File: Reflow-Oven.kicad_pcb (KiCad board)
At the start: 2 copper layers, 53 parts, among them J1 Thermocouple 1, J10 Display, J11 GND(A), J12 +12V, J13 Servo 2, J14 Servo 1, J15 Door, J17 Servo 3, J18 Ambient snesor, J19 Controls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

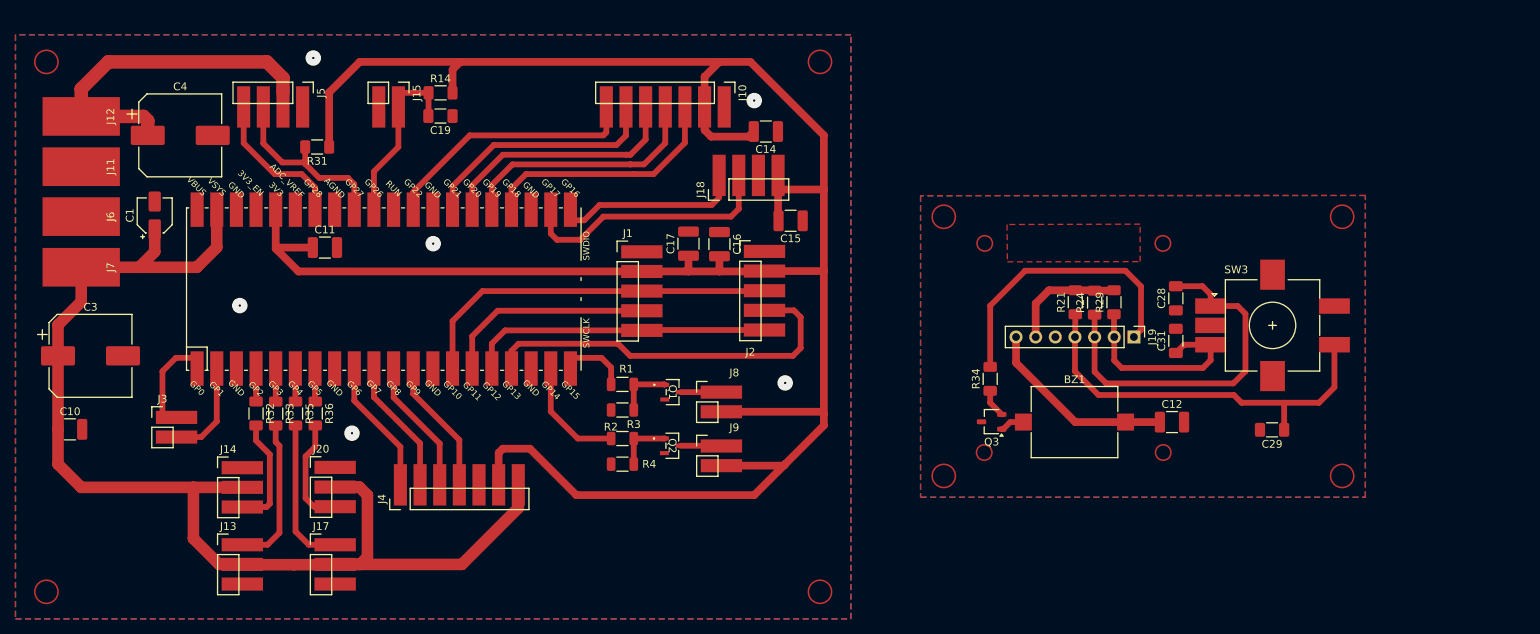
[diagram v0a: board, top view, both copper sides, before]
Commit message: Single servo with cutoff
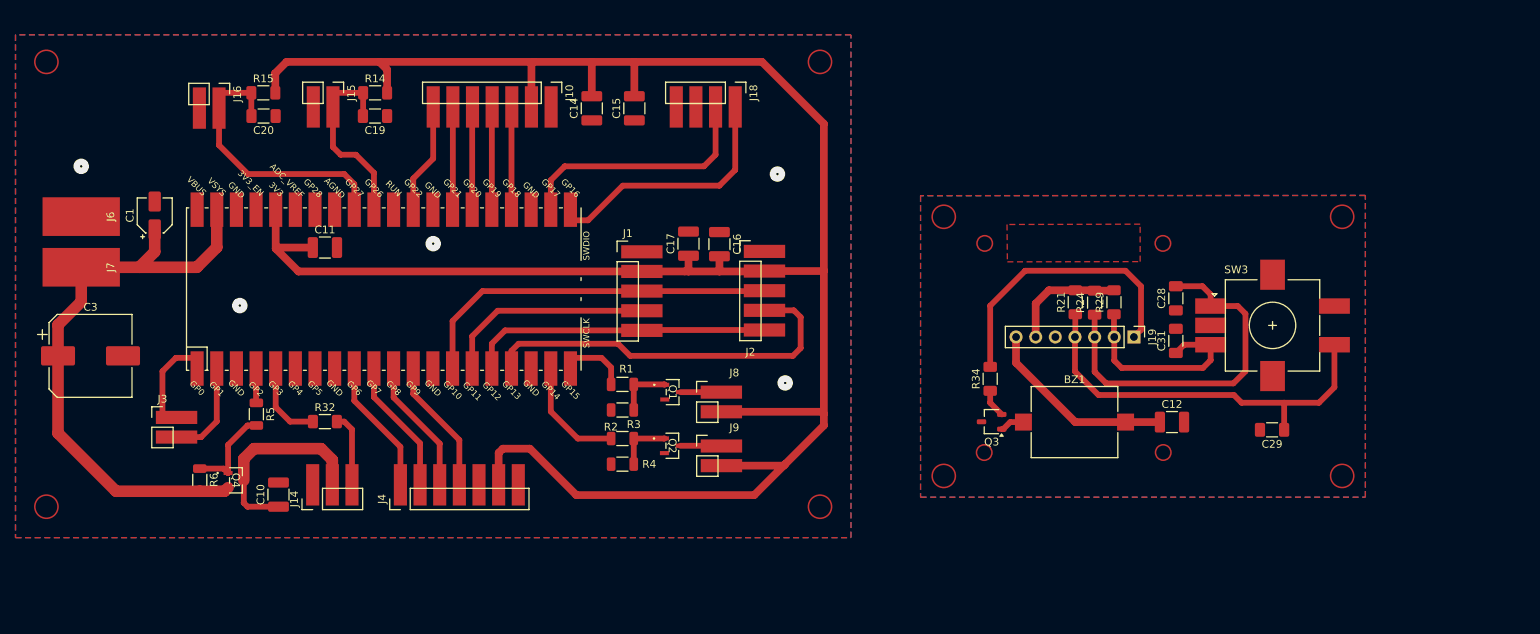
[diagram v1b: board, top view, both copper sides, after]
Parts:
- removed C4: 1000uf, Capacitor_SMD:CP_Elec_10x10.5
- removed J11: GND(A), Connector_Wire:SolderWirePad_1x01_SMD_5x10mm
- removed J12: +12V, Connector_Wire:SolderWirePad_1x01_SMD_5x10mm
- removed J13: Servo 2, Connector_PinHeader_2.54mm:PinHeader_1x03_P2.54mm_Vertical_SMD
- removed J17: Servo 3, Connector_PinHeader_2.54mm:PinHeader_1x03_P2.54mm_Vertical_SMD
- removed J20: Servo 4, Connector_PinHeader_2.54mm:PinHeader_1x03_P2.54mm_Vertical_SMD
- removed J5: Fan, Connector_PinHeader_2.54mm:PinHeader_1x04_P2.54mm_Vertical_SMD
- removed R31: 1K, Resistor_SMD:R_1206_3216Metric_Pad1.30x1.75mm_HandSolder
- removed R33, R35, R36: 220R, Resistor_SMD:R_1206_3216Metric_Pad1.30x1.75mm_HandSolder
- added C20: 10nf, Capacitor_SMD:C_1206_3216Metric_Pad1.33x1.80mm_HandSolder, F.Cu at (113.1, 58.0)
- added J16: Door, Connector_PinHeader_2.54mm:PinHeader_1x02_P2.54mm_Vertical_SMD, F.Cu at (107.3, 55.1)
- added Q4: AO3401A, PMV20XNER:SOT23-TO-236AB_NEX, F.Cu at (109.5, 105.1)
- added R15: 4K7, Resistor_SMD:R_1206_3216Metric_Pad1.30x1.75mm_HandSolder, F.Cu at (113.0, 55.0)
- added R5: 330R, Resistor_SMD:R_1206_3216Metric, F.Cu at (112.1, 96.5)
- added R6: 10K, Resistor_SMD:R_1206_3216Metric, F.Cu at (104.8, 105.0)
- moved C10 28.2 mm to (115.0, 106.9), turned to 90 degrees
- moved C15 24.9 mm to (161.0, 57.0), turned to 90 degrees
- moved C14 22.7 mm to (155.5, 57.0), turned to 90 degrees
- moved J10 22.4 mm to (150.2, 55.0)
- moved J18 12.7 mm to (174.0, 55.0), turned to -90 degrees
- moved J14 11.6 mm to (119.4, 107.5), turned to 90 degrees
- moved R32 8.96 mm to (121.0, 97.5), turned to 0 degrees
- moved C19 8.46 mm to (127.5, 58.0)
- moved J15 8.46 mm to (122.0, 55.0)
- moved R14 8.46 mm to (127.5, 55.0)
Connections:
- net /Door renamed /Door OP
- C10 pad 1: +5V -> Net-(J14-Pin_2)
- J14 pad 2: +5V -> Net-(J14-Pin_2)
- R32 pad 1: /Servo 1 -> /Servo SIG
- U1 pad 32: Net-(J5-Pin_3) -> /Door CL
- U1 pad 34: Net-(J5-Pin_4) -> unconnected-(U1-GPIO28_ADC2-Pad34)
- U1 pad 4: /Servo 1 -> /Servo EN
- U1 pad 5: /Servo 2 -> /Servo SIG
- U1 pad 6: /Servo 3 -> unconnected-(U1-GPIO4-Pad6)
- U1 pad 7: /Servo 4 -> unconnected-(U1-GPIO5-Pad7)
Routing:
- net +5V: track 177.9 -> 100.9 mm
- net +12V: track 44.6 -> 0.00 mm
- net /Door CL: track 0.00 -> 38.1 mm
- net Net-(J14-Pin_2): track 0.00 -> 28.0 mm
- net Net-(J5-Pin_3): track 27.3 -> 0.00 mm
- net Net-(J5-Pin_4): track 22.3 -> 0.00 mm
- net Net-(J13-Pin_1): track 21.3 -> 0.00 mm
- net Net-(J10-Pin_7): track 36.9 -> 17.5 mm
- net Net-(J10-Pin_4): track 35.8 -> 16.6 mm
- net Net-(J10-Pin_3): track 35.5 -> 16.6 mm
- net Net-(J10-Pin_5): track 35.5 -> 16.6 mm
- net Net-(J10-Pin_6): track 35.1 -> 16.6 mm
- net Net-(J17-Pin_1): track 17.7 -> 0.00 mm
- net Net-(J18-Pin_1): track 21.5 -> 34.0 mm
- net Net-(J20-Pin_3): track 12.4 -> 0.00 mm
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
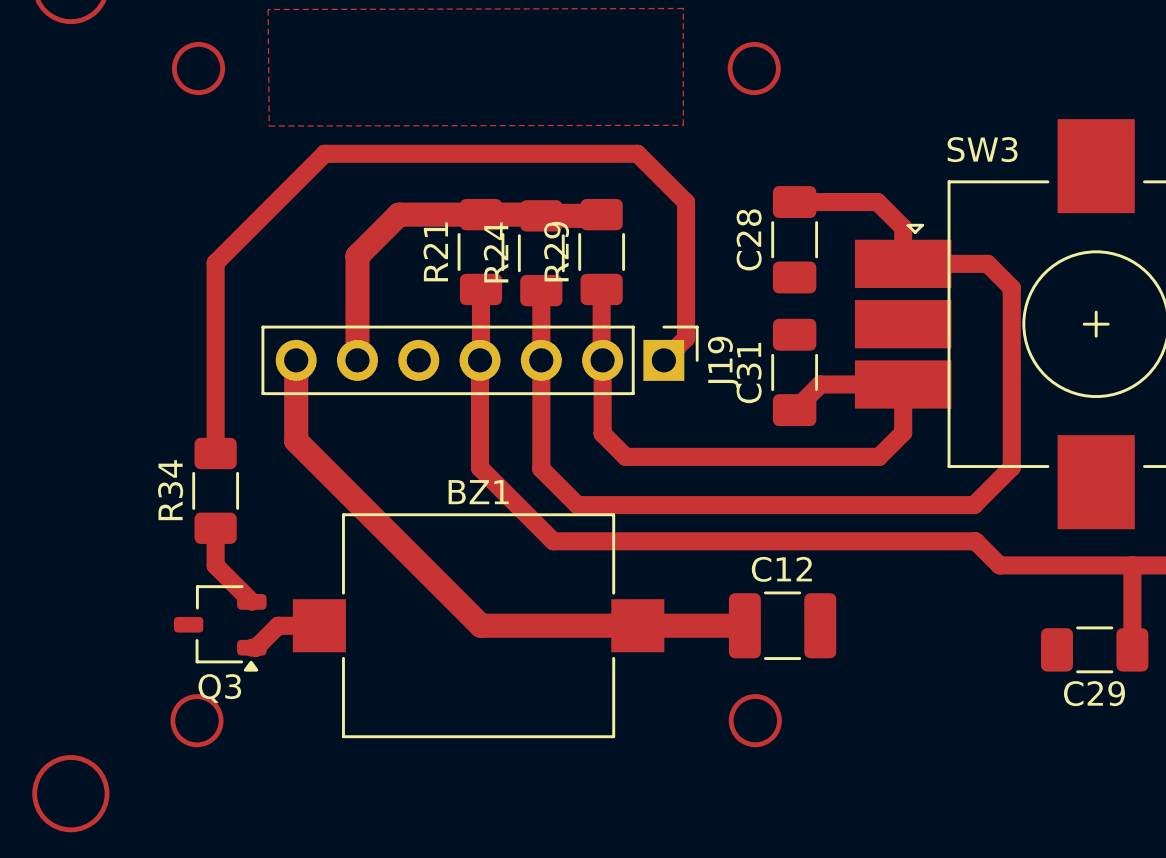
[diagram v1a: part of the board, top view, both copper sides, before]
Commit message: Single servo with cutoff
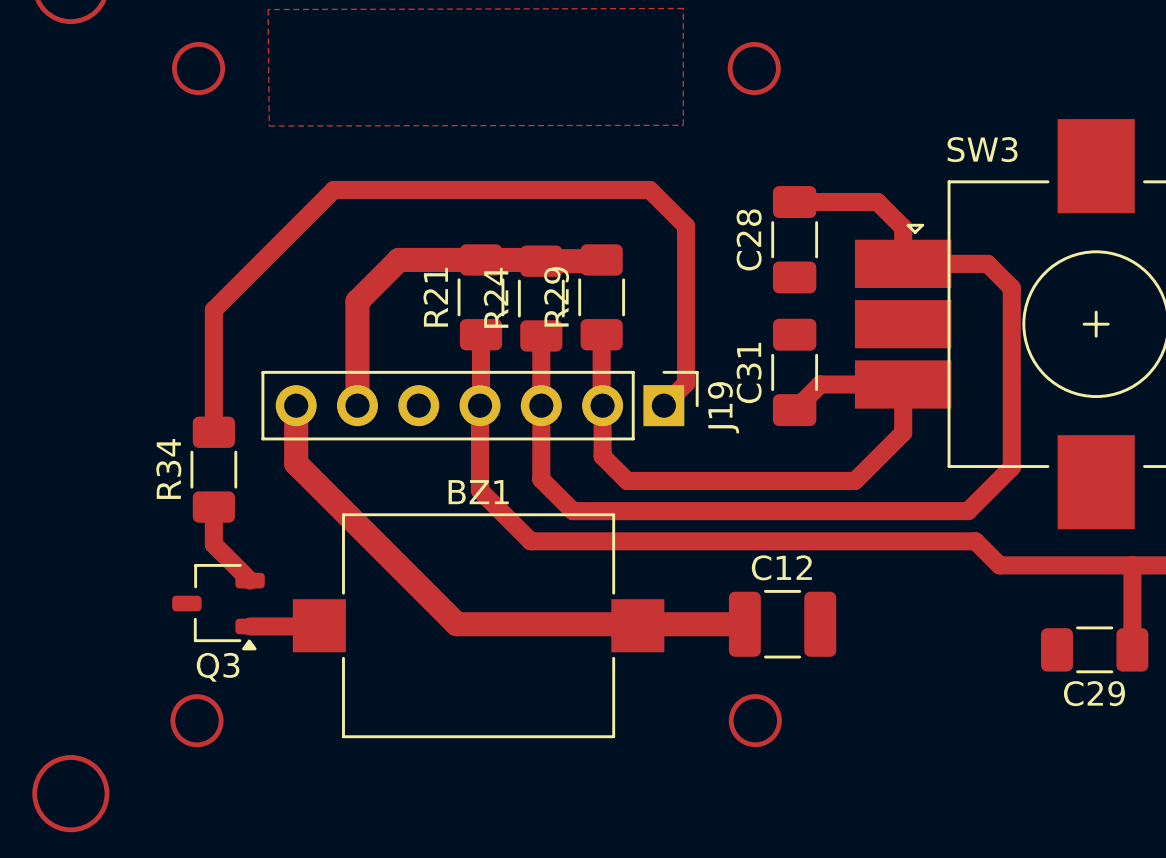
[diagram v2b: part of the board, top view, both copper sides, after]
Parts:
- moved J19 1.88 mm to (225.6, 88.4)
- moved R21 1.88 mm to (218.0, 84.0)
- moved R24 1.88 mm to (220.5, 84.0)
- moved R29 1.88 mm to (223.0, 84.0)
- moved R34 0.88 mm to (206.9, 91.1)
- moved Q3 0.88 mm to (207.1, 96.6)
- moved C12 0.06 mm to (230.5, 97.5)
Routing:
- net Net-(J19-Pin_1): track 37.0 -> 35.1 mm
- net Net-(J19-Pin_3): track 47.0 -> 45.5 mm
- net +5V: track 100.9 -> 99.5 mm
- net Net-(J19-Pin_4): track 52.5 -> 51.1 mm
- net Net-(J19-Pin_2): track 26.2 -> 25.7 mm

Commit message: Updated
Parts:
- added C18: 100nf, Capacitor_SMD:C_1210_3225Metric_Pad1.33x2.70mm_HandSolder, F.Cu at (179.4, 100.0)
- added C2: 220uf, Capacitor_SMD:CP_Elec_8x10.5, F.Cu at (177.8, 67.0)
- added C21: 100nf, Capacitor_SMD:C_1210_3225Metric_Pad1.33x2.70mm_HandSolder, F.Cu at (179.4, 93.0)
- added C4: 1000uf, Capacitor_SMD:CP_Elec_10x10.5, F.Cu at (102.0, 57.2)
- added D1: 1N5819WS, Diode_SMD:D_SOD-323_HandSoldering, F.Cu at (112.8, 51.5)
- added J11: GND(A), Connector_Wire:SolderWirePad_1x01_SMD_5x10mm, F.Cu at (89.5, 64.5)
- added J12: +12V, Connector_Wire:SolderWirePad_1x01_SMD_5x10mm, F.Cu at (89.5, 58.0)
- added J17: SSR Temp, Connector_PinHeader_2.54mm:PinHeader_1x03_P2.54mm_Vertical_SMD, F.Cu at (129.9, 55.0)
- added J20: Fan, Connector_PinHeader_2.54mm:PinHeader_1x04_P2.54mm_Vertical_SMD, F.Cu at (119.1, 55.0)
- added R16: 4K7, Resistor_SMD:R_1206_3216Metric, F.Cu at (118.0, 51.5)
- added R17: 4K7, Resistor_SMD:R_1206_3216Metric, F.Cu at (128.5, 51.5)
- J15: value Door -> Door OP
- J16: value Door -> Door CL
- J8: value Conn_01x02_Pin -> SSR1
- J9: value Conn_01x02_Pin -> SSR2
- R14, R15, R21, R24, R29, R32, R34: footprint Resistor_SMD:R_1206_3216Metric_Pad1.30x1.75mm_HandSolder -> Resistor_SMD:R_1206_3216Metric
- moved J16 55.4 mm to (125.5, 107.5), turned to 90 degrees
- moved J15 52.6 mm to (118.4, 107.5), turned to 90 degrees
- moved R14 30.0 mm to (117.2, 83.2), turned to 90 degrees
- moved R15 29.0 mm to (119.8, 83.2), turned to 90 degrees
- moved C19 28.2 mm to (114.5, 83.0), turned to -90 degrees
- moved C20 26.7 mm to (122.5, 83.0), turned to -90 degrees
- moved C12 20.6 mm to (251.1, 96.0)
- moved C28 20.6 mm to (251.6, 80.1)
- moved C31 20.6 mm to (251.6, 85.6)
- moved Q3 20.6 mm to (227.7, 95.1)
- moved R21 20.6 mm to (238.6, 82.4)
- moved R24 20.6 mm to (241.1, 82.5)
- moved R29 20.6 mm to (243.6, 82.4)
- moved R34 20.6 mm to (227.5, 89.6)
- moved BZ1 20.6 mm to (238.5, 96.1)
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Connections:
- U1 pad 31: /Door OP -> Net-(J17-Pin_2)
- U1 pad 32: /Door CL -> Net-(J20-Pin_1)
- U1 pad 34: unconnected-(U1-GPIO28_ADC2-Pad34) -> Net-(J20-Pin_2)
- U1 pad 6: unconnected-(U1-GPIO4-Pad6) -> /Door OP
- U1 pad 7: unconnected-(U1-GPIO5-Pad7) -> /Door CL
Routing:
- net +5V: track 99.5 -> 159.8 mm
- net +3.3V: track 313.5 -> 358.6 mm
- net +12V: track 0.00 -> 32.6 mm
- net Net-(J20-Pin_2): track 0.00 -> 21.3 mm
- net Net-(J17-Pin_2): track 0.00 -> 20.1 mm
- net Net-(J20-Pin_1): track 0.00 -> 18.8 mm
- net /Door CL: track 38.1 -> 28.0 mm
- net Net-(Q4-G): track 12.2 -> 22.1 mm
- net Net-(J3-Pin_1): track 11.2 -> 20.0 mm
- net Net-(J3-Pin_2): track 16.1 -> 23.5 mm
- net /Servo SIG: track 12.0 -> 5.82 mm
- net Net-(J4-Pin_4): track 20.7 -> 26.3 mm
- net Net-(J4-Pin_3): track 20.7 -> 25.7 mm
- net Net-(J4-Pin_2): track 20.7 -> 25.1 mm
- net Net-(J4-Pin_1): track 20.7 -> 25.1 mm
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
